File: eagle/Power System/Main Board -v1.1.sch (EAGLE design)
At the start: 20 parts, among them IC1 74LS14FK, IC2 74LS14FK

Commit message: PCB layout beta
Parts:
- removed C2: 6.7uF, capacitor-wima:C2.5/6
- removed D1: 1N4004, diode:1N4004
- removed IC1, IC2: 74LS14FK, 74xx-eu:74LS14FK
- removed R7: 4.7K, rcl:R-US_0207/7
- removed S2: 5501, switch:5501
- removed U$1: F552X---PN80, TI_MSP430_v16:F552X---PN80
- added SV7: MSP430 - LEFT, con-lsta:FE10-2
- added SV8: MSP430 - RIGHT, con-lsta:FE10-2
- SV1: value (none) -> JSN-SR04 FRONT
- SV12: value (none) -> To Notification panel
- SV2: value (none) -> JSN-SR04 LEFT
- SV3: value (none) -> JSN-SR04 RIGHT
- SV4: value (none) -> MPU9250
- SV5: value (none) -> HC-06
- SV6: value (none) -> Motor communication\
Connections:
- removed net N$16: IC2A.O, U$1.76
- removed net N$2: D1.A, S2.1A
- removed net N$22: U$1.42
- removed net N$23: C2.1, IC1A.I, R7.1
- removed net N$3: IC1A.O, IC2A.I
- net +3V3: now also SV7.19; no longer D1.C, R7.2
- net GND: now also SV7.18, SV8.20; no longer C2.2, S2.NC
- net N$10: now also SV8.9; no longer U$1.23
- net N$11: now also SV8.11; no longer U$1.24
- net N$12: now also SV8.17; no longer U$1.33
- net N$13: now also SV7.16; no longer U$1.77
- net N$14: now also SV8.8; no longer U$1.38
- net N$15: now also SV7.13; no longer U$1.40
- net N$18: now also SV8.16; no longer U$1.31
- net N$20: now also SV8.4; no longer U$1.32
- net N$21: now also SV8.18; no longer U$1.29
- net N$24: now also SV8.15; no longer U$1.26
- net N$25: now also SV8.3; no longer U$1.44
- net N$26: now also SV7.15; no longer U$1.41
- net N$27: now also SV8.5; no longer U$1.45
- net N$28: now also SV8.7; no longer U$1.48
- net N$30: now also SV7.4; no longer U$1.43
- net N$4: now also SV8.10; no longer U$1.37
- net N$5: now also SV8.19; no longer U$1.34
- net N$6: now also SV8.2; no longer U$1.16
- net N$8: now also SV8.1; no longer U$1.17
- net N$9: now also SV7.14; no longer U$1.78
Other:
- note removed: "Power On Circiut"

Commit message: updated pcb
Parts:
- added SV10: (no value), con-lsta:FE12-1
- added SV9: (no value), con-lsta:FE20-1
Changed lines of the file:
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@@
 <?xml version="1.0" encoding="utf-8"?>
 <!DOCTYPE eagle SYSTEM "eagle.dtd">
-<eagle version="7.5.0">
+<eagle version="7.3.0">
 <drawing>
 <settings>
@@
 <part name="GND9" library="supply1" deviceset="GND" device=""/>
 <part name="GND11" library="supply1" deviceset="GND" device=""/>
+<part name="SV9" library="con-lsta" deviceset="FE20-1" device=""/>
+<part name="SV10" library="con-lsta" deviceset="FE12-1" device=""/>
 </parts>
 <sheets>
@@
 <instance part="GND9" gate="1" x="58.42" y="177.8" rot="R90"/>
 <instance part="GND11" gate="1" x="27.94" y="193.04" rot="R180"/>
+<instance part="SV9" gate="G$1" x="160.02" y="170.18"/>
+<instance part="SV10" gate="G$1" x="137.16" y="172.72"/>
 </instances>
 <busses>

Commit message: resized main board
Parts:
- removed SV10: (no value), con-lsta:FE12-1
- removed SV9: (no value), con-lsta:FE20-1
- added SV14: JSN-SR04 BACK, con-lstb:MA04-1
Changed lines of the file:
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@@
 <part name="GND9" library="supply1" deviceset="GND" device=""/>
 <part name="GND11" library="supply1" deviceset="GND" device=""/>
-<part name="SV9" library="con-lsta" deviceset="FE20-1" device=""/>
-<part name="SV10" library="con-lsta" deviceset="FE12-1" device=""/>
+<part name="SV14" library="con-lstb" deviceset="MA04-1" device="" value="JSN-SR04 BACK"/>
 </parts>
 <sheets>
@@
 <instance part="GND9" gate="1" x="58.42" y="177.8" rot="R90"/>
 <instance part="GND11" gate="1" x="27.94" y="193.04" rot="R180"/>
-<instance part="SV9" gate="G$1" x="160.02" y="170.18"/>
-<instance part="SV10" gate="G$1" x="137.16" y="172.72"/>
+<instance part="SV14" gate="1" x="180.34" y="218.44"/>
 </instances>
 <busses>

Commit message: final pcb versions
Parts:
- SV1: value JSN-SR04 FRONT -> JSN-SR04
- SV14: value JSN-SR04 BACK -> JSN-SR04
- SV2: value JSN-SR04 LEFT -> JSN-SR04
- SV3: value JSN-SR04 RIGHT -> JSN-SR04
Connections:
- net N$27: now also SV12.7; no longer SV12.6
- net N$28: now also SV12.6; no longer SV12.7
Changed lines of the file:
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@@
 <?xml version="1.0" encoding="utf-8"?>
 <!DOCTYPE eagle SYSTEM "eagle.dtd">
-<eagle version="7.3.0">
+<eagle version="7.5.0">
 <drawing>
 <settings>
@@
 <part name="GND10" library="supply1" deviceset="GND" device=""/>
 <part name="SV5" library="con-lstb" deviceset="MA04-1" device="" value="HC-06"/>
-<part name="SV1" library="con-lstb" deviceset="MA04-1" device="" value="JSN-SR04 FRONT"/>
-<part name="SV2" library="con-lstb" deviceset="MA04-1" device="" value="JSN-SR04 LEFT"/>
-<part name="SV3" library="con-lstb" deviceset="MA04-1" device="" value="JSN-SR04 RIGHT"/>
+<part name="SV1" library="con-lstb" deviceset="MA04-1" device="" value="JSN-SR04 "/>
+<part name="SV2" library="con-lstb" deviceset="MA04-1" device="" value="JSN-SR04 "/>
+<part name="SV3" library="con-lstb" deviceset="MA04-1" device="" value="JSN-SR04 "/>
 <part name="P+3" library="supply1" deviceset="+5V" device=""/>
 <part name="FRAME2" library="frames" deviceset="FRAME_B_L" device=""/>
@@
 <part name="GND9" library="supply1" deviceset="GND" device=""/>
 <part name="GND11" library="supply1" deviceset="GND" device=""/>
-<part name="SV14" library="con-lstb" deviceset="MA04-1" device="" value="JSN-SR04 BACK"/>
+<part name="SV14" library="con-lstb" deviceset="MA04-1" device="" value="JSN-SR04 "/>
 </parts>
 <sheets>
@@
 <net name="N$27" class="0">
 <segment>
-<pinref part="SV12" gate="G$1" pin="6"/>
-<wire x1="132.08" y1="254" x2="132.08" y2="223.52" width="0.1524" layer="91"/>
-<wire x1="132.08" y1="223.52" x2="12.7" y2="223.52" width="0.1524" layer="91"/>
+<wire x1="134.62" y1="223.52" x2="12.7" y2="223.52" width="0.1524" layer="91"/>
 <wire x1="12.7" y1="223.52" x2="12.7" y2="160.02" width="0.1524" layer="91"/>
 <pinref part="SV8" gate="G$1" pin="5"/>
 <wire x1="12.7" y1="160.02" x2="33.02" y2="160.02" width="0.1524" layer="91"/>
+<pinref part="SV12" gate="G$1" pin="7"/>
+<wire x1="134.62" y1="223.52" x2="134.62" y2="254" width="0.1524" layer="91"/>
 </segment>
 </net>
 <net name="N$28" class="0">
 <segment>
-<pinref part="SV12" gate="G$1" pin="7"/>
-<wire x1="134.62" y1="218.44" x2="134.62" y2="254" width="0.1524" layer="91"/>
-<wire x1="134.62" y1="218.44" x2="18.034" y2="218.44" width="0.1524" layer="91"/>
+<wire x1="132.08" y1="218.44" x2="18.034" y2="218.44" width="0.1524" layer="91"/>
 <wire x1="18.034" y1="218.44" x2="18.034" y2="163.068" width="0.1524" layer="91"/>
 <pinref part="SV8" gate="G$1" pin="7"/>
 <wire x1="18.034" y1="163.068" x2="33.02" y2="163.068" width="0.1524" layer="91"/>
 <wire x1="33.02" y1="163.068" x2="33.02" y2="162.56" width="0.1524" layer="91"/>
-</segment>
-</net>
+<pinref part="SV12" gate="G$1" pin="6"/>
+<wire x1="132.08" y1="218.44" x2="132.08" y2="254" width="0.1524" layer="91"/>
+</segment>
+</net>

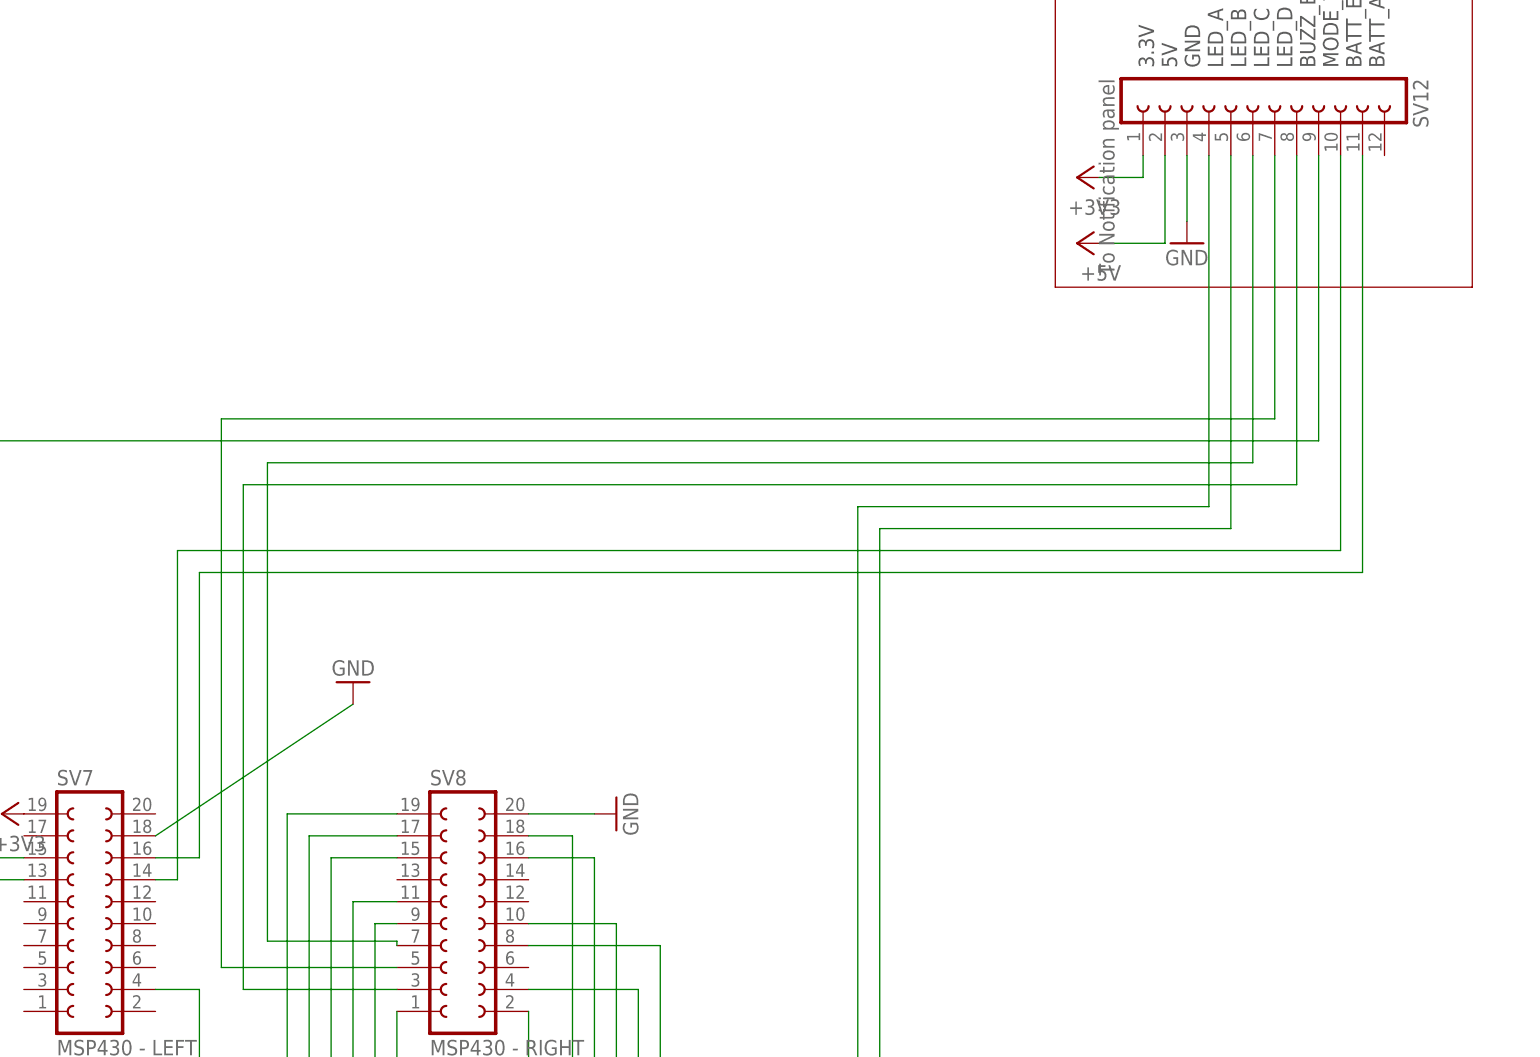
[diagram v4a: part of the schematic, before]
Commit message: added multimeter
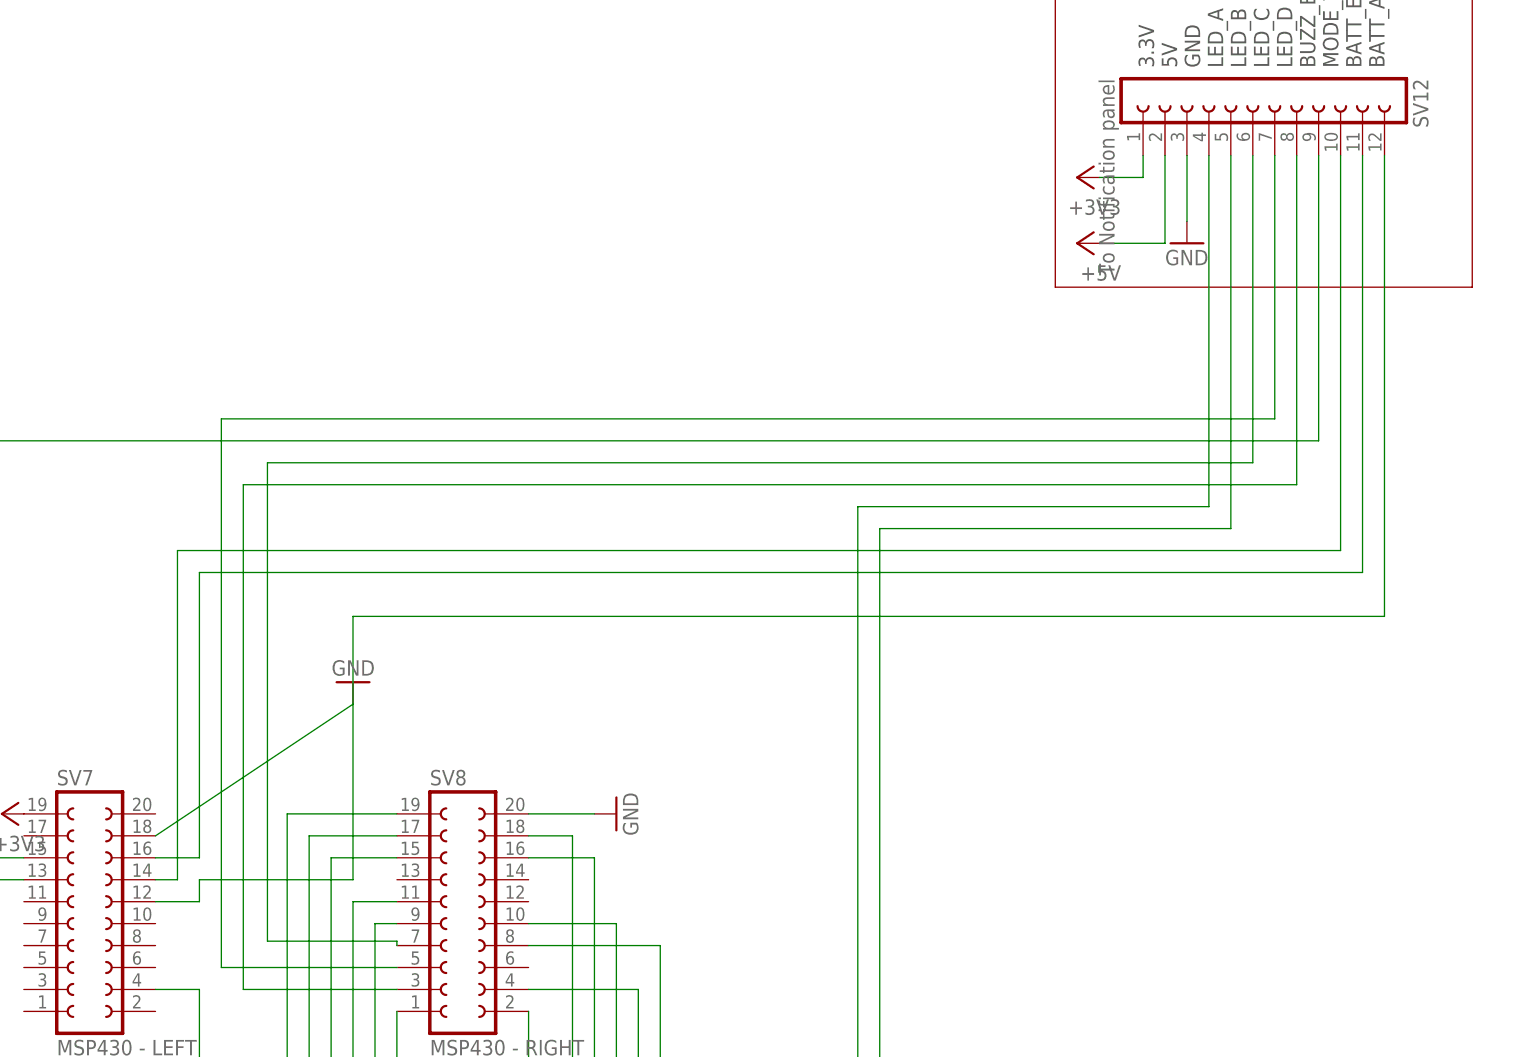
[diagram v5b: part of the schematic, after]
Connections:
- new net N$2: SV12.12, SV7.12
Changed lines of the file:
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@@
 <?xml version="1.0" encoding="utf-8"?>
 <!DOCTYPE eagle SYSTEM "eagle.dtd">
-<eagle version="7.5.0">
+<eagle version="7.3.0">
 <drawing>
 <settings>
@@
 </segment>
 </net>
+<net name="N$2" class="0">
+<segment>
+<pinref part="SV12" gate="G$1" pin="12"/>
+<wire x1="147.32" y1="254" x2="147.32" y2="200.66" width="0.1524" layer="91"/>
+<wire x1="147.32" y1="200.66" x2="27.94" y2="200.66" width="0.1524" layer="91"/>
+<wire x1="27.94" y1="200.66" x2="27.94" y2="170.18" width="0.1524" layer="91"/>
+<wire x1="27.94" y1="170.18" x2="10.16" y2="170.18" width="0.1524" layer="91"/>
+<wire x1="10.16" y1="170.18" x2="10.16" y2="167.64" width="0.1524" layer="91"/>
+<pinref part="SV7" gate="G$1" pin="12"/>
+<wire x1="10.16" y1="167.64" x2="5.08" y2="167.64" width="0.1524" layer="91"/>
+</segment>
+</net>

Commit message: last push
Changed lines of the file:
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@@
 <instance part="+3V1" gate="G$1" x="-12.7" y="177.8" rot="R90"/>
 <instance part="GND9" gate="1" x="58.42" y="177.8" rot="R90"/>
-<instance part="GND11" gate="1" x="27.94" y="193.04" rot="R180"/>
+<instance part="GND11" gate="1" x="22.86" y="182.88" rot="R180"/>
 <instance part="SV14" gate="1" x="180.34" y="218.44"/>
 </instances>
@@
 <pinref part="SV7" gate="G$1" pin="18"/>
 <pinref part="GND11" gate="1" pin="GND"/>
-<wire x1="27.94" y1="190.5" x2="5.08" y2="175.26" width="0.1524" layer="91"/>
+<wire x1="22.86" y1="180.34" x2="5.08" y2="175.26" width="0.1524" layer="91"/>
 </segment>
 </net>
